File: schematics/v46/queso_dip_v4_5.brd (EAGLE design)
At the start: 41 x 50 mm, 50 parts, among them Q1 FOXSDLF/120-20, U1 PRTR5V0U2X,215, U2 PRTR5V0U2X,215, U3 PRTR5V0U2X,215, U4 PRTR5V0U2X,215, U5 PRTR5V0U2X,215, X1 USB-A-HU, X2 USB-A-HU, X3 USB-A-HU, X4 USB-A-HU

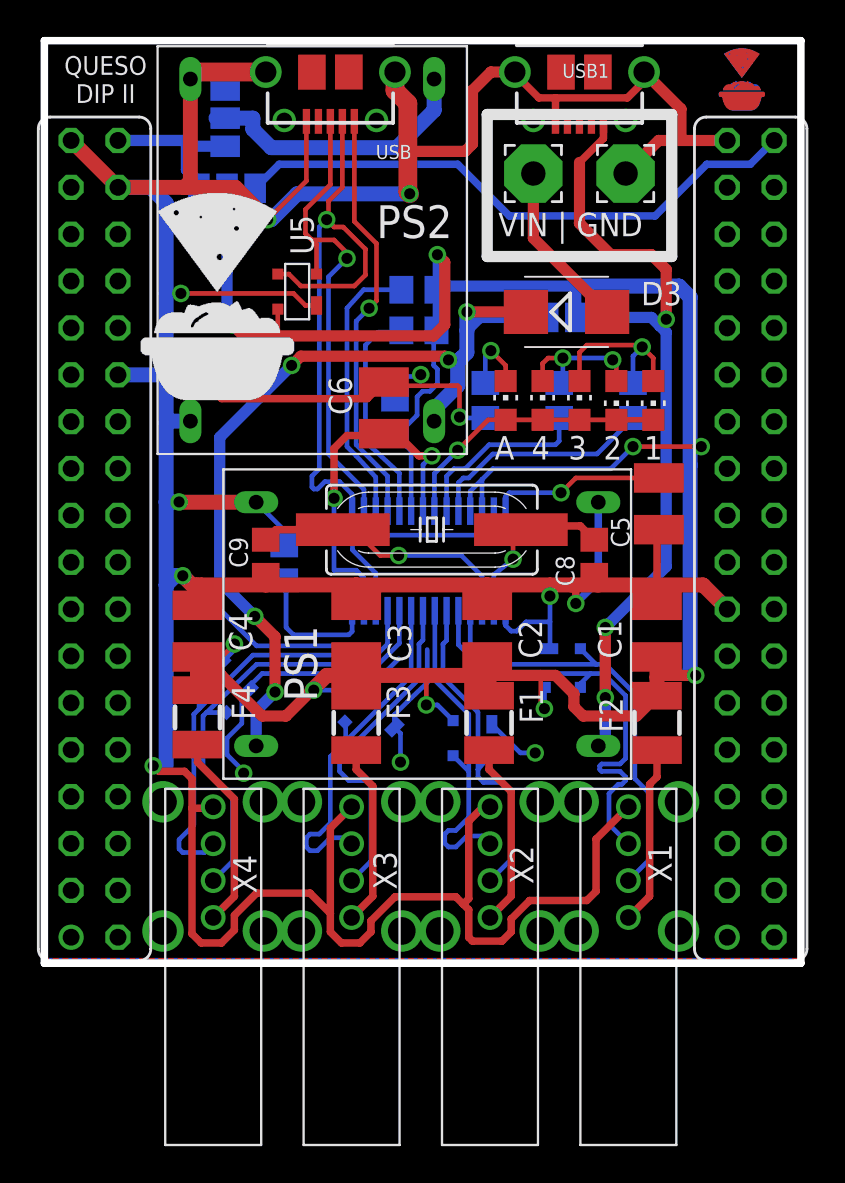
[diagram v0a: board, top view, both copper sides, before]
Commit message: added flat usb version
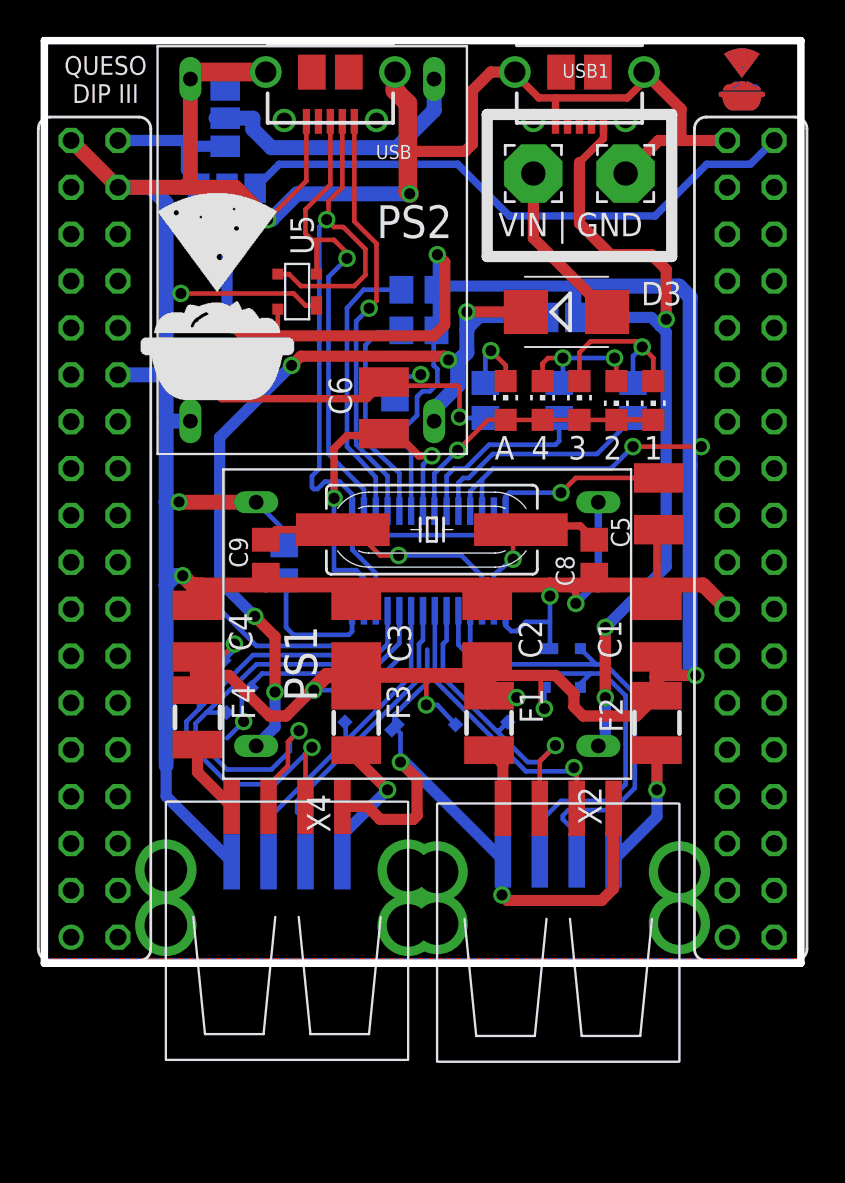
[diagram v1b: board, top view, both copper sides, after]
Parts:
- X1, X2, X3, X4: value USB-A-HU -> USB-A-S; device con-usb:USB-A-HU -> con-usb:USB-A-S
- moved X4 5.19 mm to (13.2, 5.05)
- moved X2 4.89 mm to (27.9, 4.95)
- moved X1 3.82 mm to (27.9, 2.15), flipped to the bottom
- moved X3 3.51 mm to (13.2, 2.05), flipped to the bottom
- moved U2 0.94 mm to (23.7, 13.0), turned to 225 degrees
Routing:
- net GND: track 305.4 -> 275.1 mm
- net N$4: track 10.0 -> 3.46 mm
- net N$3: track 10.7 -> 4.12 mm
- net DP1: track 24.9 -> 28.8 mm, vias 0 -> 1
- net DM1: track 25.1 -> 28.8 mm, vias 0 -> 1
- net N$1: track 9.71 -> 6.92 mm, vias 0 -> 1
- net N$5: track 9.92 -> 7.77 mm, vias 0 -> 1
- net DM3: track 18.4 -> 16.6 mm, vias 0 -> 1
- net DP3: track 18.3 -> 16.6 mm, vias 0 -> 1
- net DP2: track 19.5 -> 17.9 mm
- net DM2: track 19.4 -> 17.9 mm
- net DM4: track 24.0 -> 25.4 mm
- net DP4: track 24.3 -> 25.4 mm
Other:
- board text added: "QUESO DIP III"
- board text removed: "QUESO DIP II"
